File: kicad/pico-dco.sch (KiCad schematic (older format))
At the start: 28 parts

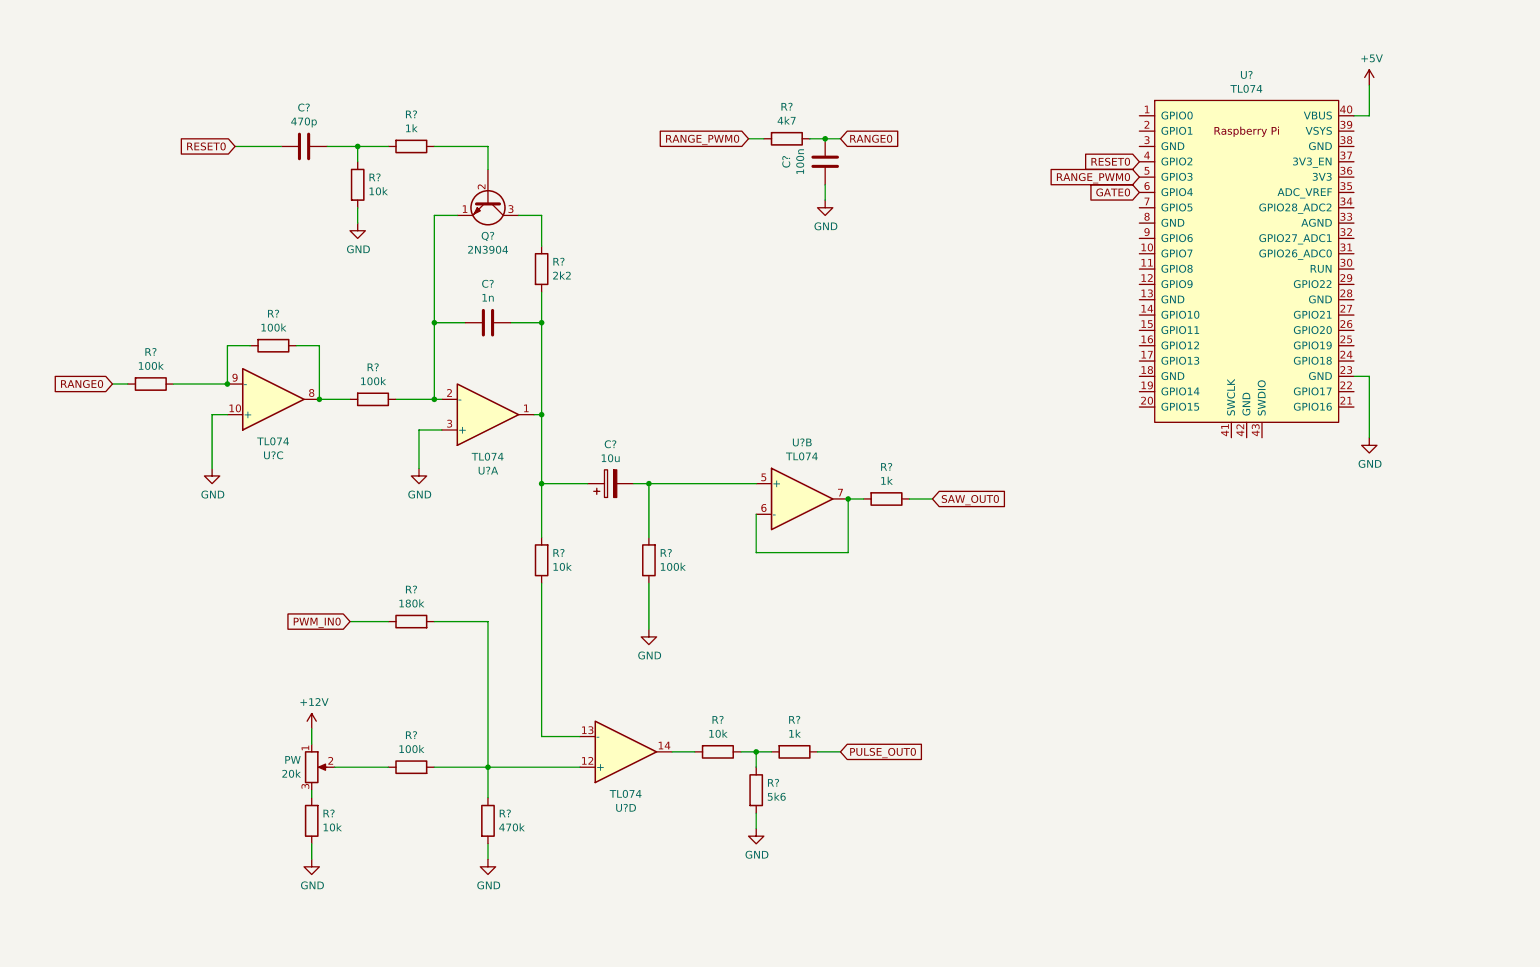
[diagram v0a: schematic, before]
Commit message: Add 6 voices and serial midi to kicad schematics/PCB
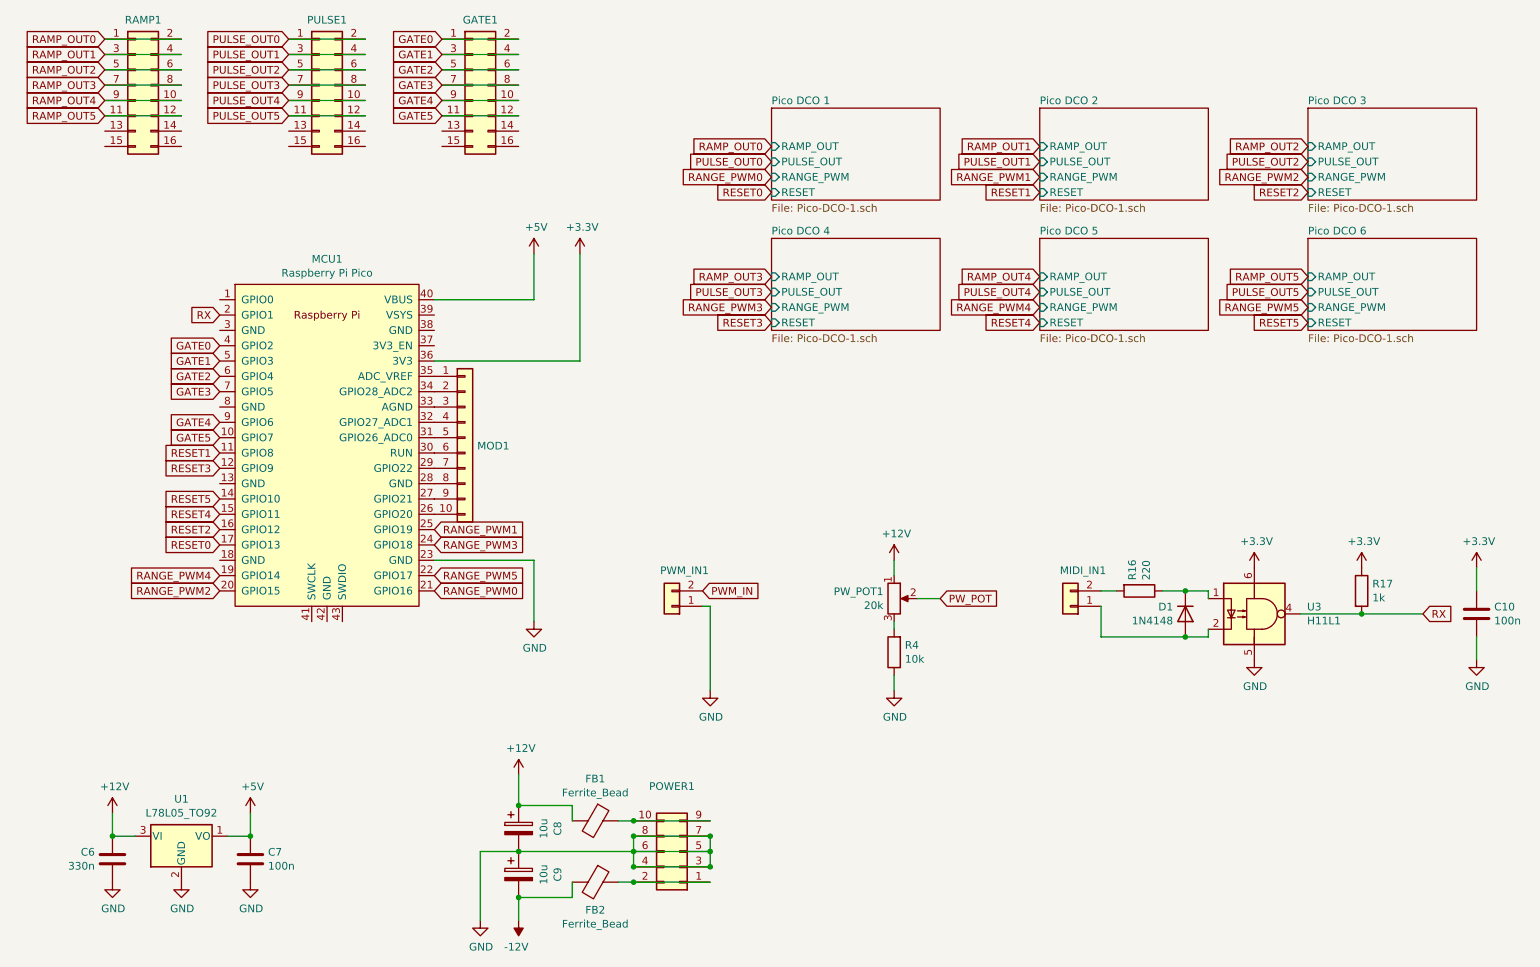
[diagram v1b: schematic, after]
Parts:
- removed C?: 1n, symbol Device:C
- removed C?: 470p, symbol Device:C
- removed C?: 10u, symbol Device:CP
- removed C?: 100n, symbol Device:C
- removed PW: 20k, symbol Device:R_POT
- removed Q?: 2N3904, Package_TO_SOT_THT:TO-92_Inline, symbol Transistor_BJT:2N3904
- removed R?: 2k2, symbol Device:R
- removed R? (x3): 1k, symbol Device:R
- removed R? (x4): 10k, symbol Device:R
- removed R? (x5): 100k, symbol Device:R
- removed R?: 470k, symbol Device:R
- removed R?: 180k, symbol Device:R
- removed R?: 5k6, symbol Device:R
- removed R?: 4k7, symbol Device:R
- removed U? (x4): TL074, symbol Amplifier_Operational:TL074
- added C10, C7: 100n, Capacitor_THT:C_Rect_L7.2mm_W4.5mm_P5.00mm_FKS2_FKP2_MKS2_MKP2, symbol Device:C
- added C6: 330n, Capacitor_THT:C_Rect_L7.2mm_W4.5mm_P5.00mm_FKS2_FKP2_MKS2_MKP2, symbol Device:C
- added C8, C9: 10u, Capacitor_THT:CP_Radial_D5.0mm_P2.00mm, symbol Device:CP
- added D1: 1N4148, Diode_THT:D_DO-35_SOD27_P7.62mm_Horizontal, symbol Diode:1N4148
- added FB1, FB2: Ferrite_Bead, Resistor_THT:R_Axial_DIN0207_L6.3mm_D2.5mm_P10.16mm_Horizontal, symbol Device:Ferrite_Bead
- added GATE1, PULSE1, RAMP1: Conn_02x08_Odd_Even, Connector_IDC:IDC-Header_2x08_P2.54mm_Vertical, symbol Connector_Generic:Conn_02x08_Odd_Even
- added MIDI_IN1, PWM_IN1: Conn_01x02, Connector_Molex:Molex_KK-254_AE-6410-02A_1x02_P2.54mm_Vertical, symbol Connector_Generic:Conn_01x02
- added MOD1: Conn_01x10, Connector_PinHeader_2.54mm:PinHeader_1x10_P2.54mm_Vertical, symbol Connector_Generic:Conn_01x10
- added POWER1: Conn_02x05_Odd_Even, Connector_IDC:IDC-Header_2x05_P2.54mm_Vertical, symbol Connector_Generic:Conn_02x05_Odd_Even
- added PW_POT1: 20k, Connector_Molex:Molex_KK-254_AE-6410-03A_1x03_P2.54mm_Vertical, symbol Device:R_POT
- added R16: 220, Resistor_THT:R_Axial_DIN0207_L6.3mm_D2.5mm_P10.16mm_Horizontal, symbol Device:R
- added R17: 1k, Resistor_THT:R_Axial_DIN0207_L6.3mm_D2.5mm_P10.16mm_Horizontal, symbol Device:R
- added R4: 10k, Resistor_THT:R_Axial_DIN0207_L6.3mm_D2.5mm_P10.16mm_Horizontal, symbol Device:R
- added U1: L78L05_TO92, Package_TO_SOT_THT:TO-92_Wide, symbol Regulator_Linear:L78L05_TO92
- added U3: H11L1, Package_DIP:DIP-6_W7.62mm_Socket_LongPads, symbol Isolator:H11L1
- MCU1: renamed from U?; value TL074 -> Raspberry Pi Pico; footprint (none) -> RPi_Pico:RPi_Pico_SMD_TH
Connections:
- net +12V: now also C6.2, C8.1, FB1.2, PW_POT1.1, U1.3 (VI)
- net +5V: now also C7.1, U1.1 (VO)
- net GATE0: now also MCU1.4 (GPIO2), GATE1.1 (Pin_1), GATE1.2 (Pin_2); no longer MCU1.6 (GPIO4)
- net GND: now also C10.2, C6.1, C7.2, C8.2, C9.1, POWER1.3 (Pin_3), POWER1.4 (Pin_4), POWER1.5 (Pin_5), POWER1.6 (Pin_6), POWER1.7 (Pin_7), POWER1.8 (Pin_8), PWM_IN1.1 (Pin_1), R4.1, U1.2 (GND), U3.5
- net PULSE_OUT0: now also PULSE1.1 (Pin_1), PULSE1.2 (Pin_2)
- net RANGE_PWM0: now also MCU1.21 (GPIO16); no longer MCU1.5 (GPIO3)
- net RESET0: now also MCU1.17 (GPIO13); no longer MCU1.4 (GPIO2)
- net GATE5: now reaches MCU1.10 (GPIO7)
- net GATE5: now also GATE1.11 (Pin_11), GATE1.12 (Pin_12)
- net RESET1: now reaches MCU1.11 (GPIO8)
- net RESET3: now reaches MCU1.12 (GPIO9)
- net RESET5: now reaches MCU1.14 (GPIO10)
- net RESET4: now reaches MCU1.15 (GPIO11)
- net RESET2: now reaches MCU1.16 (GPIO12)
- net RANGE_PWM4: now reaches MCU1.19 (GPIO14)
- net RX: now reaches MCU1.2 (GPIO1)
- net RX: now also R17.2, U3.4
- net RANGE_PWM2: now reaches MCU1.20 (GPIO15)
- net RANGE_PWM5: now reaches MCU1.22 (GPIO17)
- net RANGE_PWM3: now reaches MCU1.24 (GPIO18)
- net RANGE_PWM1: now reaches MCU1.25 (GPIO19)
- net at MCU1.26 (GPIO20): now also MOD1.10 (Pin_10)
- net at MCU1.27 (GPIO21): now also MOD1.9 (Pin_9)
- net at MCU1.28 (GND): now also MOD1.8 (Pin_8)
- net at MCU1.29 (GPIO22): now also MOD1.7 (Pin_7)
- net at MCU1.30 (RUN): now also MOD1.6 (Pin_6)
- net at MCU1.31 (GPIO26_ADC0): now also MOD1.5 (Pin_5)
- net at MCU1.32 (GPIO27_ADC1): now also MOD1.4 (Pin_4)
- net at MCU1.33 (AGND): now also MOD1.3 (Pin_3)
- net at MCU1.34 (GPIO28_ADC2): now also MOD1.2 (Pin_2)
- net at MCU1.35 (ADC_VREF): now also MOD1.1 (Pin_1)
- net +3V3: now reaches MCU1.36 (3V3)
- net +3V3: now also C10.1, R17.1, U3.6
- net GATE3: now reaches MCU1.7 (GPIO5)
- net GATE3: now also GATE1.7 (Pin_7), GATE1.8 (Pin_8)
- net GATE4: now reaches MCU1.9 (GPIO6)
- net GATE4: now also GATE1.10 (Pin_10), GATE1.9 (Pin_9)
- new net: PW_POT1.3, R4.2
- new net: D1.1 (K), R16.1, U3.1
- new net: D1.2 (A), MIDI_IN1.1 (Pin_1), U3.2
- new net: MIDI_IN1.2 (Pin_2), R16.2
- new net: FB2.1, POWER1.1 (Pin_1), POWER1.2 (Pin_2)
- new net: FB1.1, POWER1.10 (Pin_10), POWER1.9 (Pin_9)
- new net -12V: C9.2, FB2.2
- new net GATE1: GATE1.3 (Pin_3), GATE1.4 (Pin_4), MCU1.5 (GPIO3)
- new net GATE2: GATE1.5 (Pin_5), GATE1.6 (Pin_6), MCU1.6 (GPIO4)
- new net PULSE_OUT1: PULSE1.3 (Pin_3), PULSE1.4 (Pin_4)
- new net PULSE_OUT2: PULSE1.5 (Pin_5), PULSE1.6 (Pin_6)
- new net PULSE_OUT3: PULSE1.7 (Pin_7), PULSE1.8 (Pin_8)
- new net PULSE_OUT4: PULSE1.10 (Pin_10), PULSE1.9 (Pin_9)
- new net PULSE_OUT5: PULSE1.11 (Pin_11), PULSE1.12 (Pin_12)
- new net PWM_IN: PWM_IN1.2 (Pin_2)
- new net PW_POT: PW_POT1.2
- new net RAMP_OUT0: RAMP1.1 (Pin_1), RAMP1.2 (Pin_2)
- new net RAMP_OUT1: RAMP1.3 (Pin_3), RAMP1.4 (Pin_4)
- new net RAMP_OUT2: RAMP1.5 (Pin_5), RAMP1.6 (Pin_6)
- new net RAMP_OUT3: RAMP1.7 (Pin_7), RAMP1.8 (Pin_8)
- new net RAMP_OUT4: RAMP1.10 (Pin_10), RAMP1.9 (Pin_9)
- new net RAMP_OUT5: RAMP1.11 (Pin_11), RAMP1.12 (Pin_12)
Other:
- moved on the sheet: MCU1

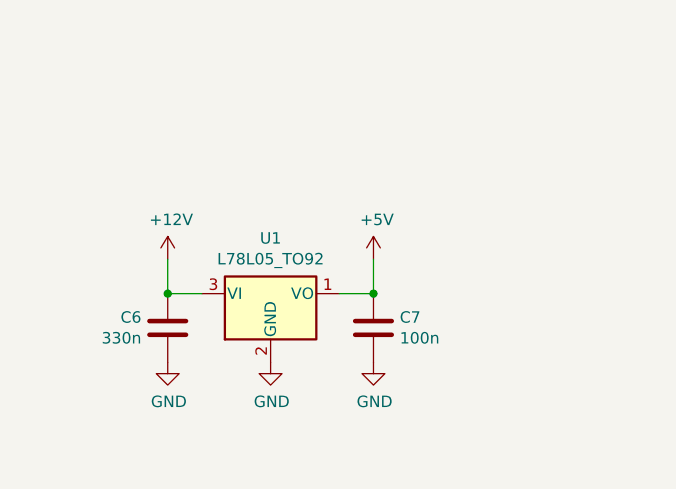
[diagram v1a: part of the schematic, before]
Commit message: Changed 5V regulator to L7805
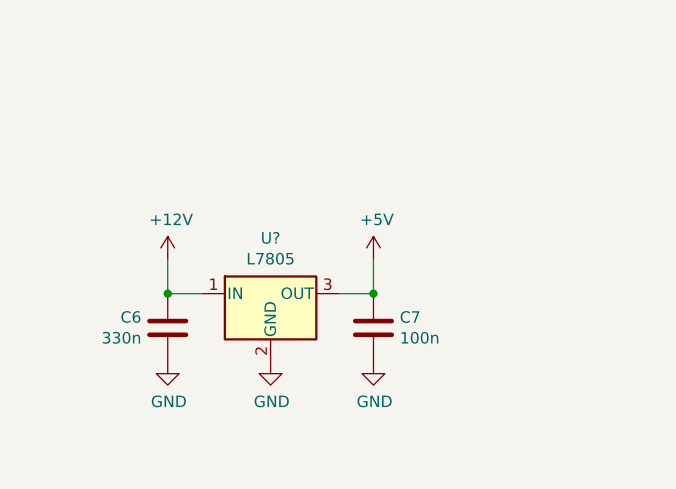
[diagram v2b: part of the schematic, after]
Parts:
- removed U1: L78L05_TO92, Package_TO_SOT_THT:TO-92_Wide, symbol Regulator_Linear:L78L05_TO92
- added U?: L7805, Package_TO_SOT_THT:TO-220-3_Vertical, symbol Regulator_Linear:L7805
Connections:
- net +12V: now also U?.1 (IN)
- net +5V: now also U?.3 (OUT)
- net GND: now also U?.2 (GND)
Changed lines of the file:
@@
 	6700 4850 6850 4850
-$Comp
-L Regulator_Linear:L78L05_TO92 U1
-U 1 1 60963782
-P 1900 6400
-F 0 "U1" H 1900 6642 50  0000 C CNN
-F 1 "L78L05_TO92" H 1900 6551 50  0000 C CNN
-F 2 "Package_TO_SOT_THT:TO-92_Wide" H 1900 6625 50  0001 C CIN
-F 3 "http://www.st.com/content/ccc/resource/technical/document/datasheet/15/55/e5/aa/23/5b/43/fd/CD00000446.pdf/files/CD00000446.pdf/jcr:content/translations/en.CD00000446.pdf" H 1900 6350 50  0001 C CNN
-	1    1900 6400
-	1    0    0    -1
-$EndComp
 $Comp
 L power:GND #PWR0114
@@
 	1    0    0    -1
 $EndComp
+$Comp
+L Regulator_Linear:L7805 U?
+U 1 1 61096C61
+P 1900 6400
+F 0 "U?" H 1900 6642 50  0000 C CNN
+F 1 "L7805" H 1900 6551 50  0000 C CNN
+F 2 "Package_TO_SOT_THT:TO-220-3_Vertical" H 1925 6250 50  0001 L CIN
+F 3 "http://www.st.com/content/ccc/resource/technical/document/datasheet/41/4f/b3/b0/12/d4/47/88/CD00000444.pdf/files/CD00000444.pdf/jcr:content/translations/en.CD00000444.pdf" H 1900 6350 50  0001 C CNN
+	1    1900 6400
+	1    0    0    -1
+$EndComp

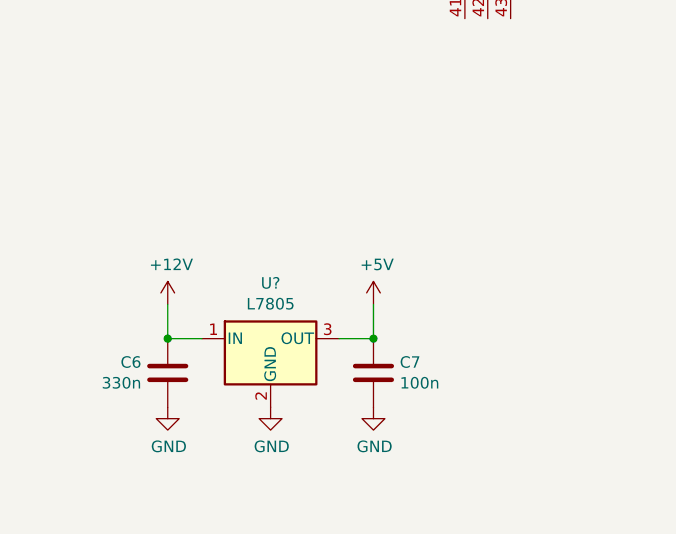
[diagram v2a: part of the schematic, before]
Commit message: Add polyphony, update readme
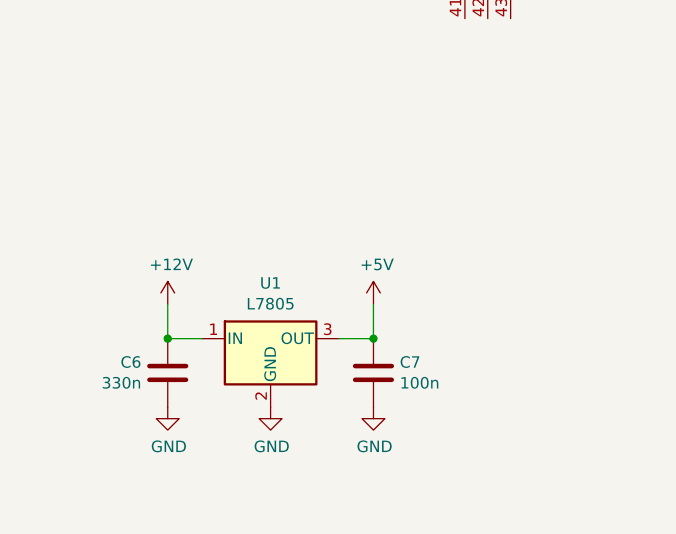
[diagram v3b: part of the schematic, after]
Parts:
- gave numbers to parts that had none: 1
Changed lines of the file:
@@
 $EndComp
 $Comp
-L Regulator_Linear:L7805 U?
+L Regulator_Linear:L7805 U1
 U 1 1 61096C61
 P 1900 6400
-F 0 "U?" H 1900 6642 50  0000 C CNN
+F 0 "U1" H 1900 6642 50  0000 C CNN
 F 1 "L7805" H 1900 6551 50  0000 C CNN
 F 2 "Package_TO_SOT_THT:TO-220-3_Vertical" H 1925 6250 50  0001 L CIN
